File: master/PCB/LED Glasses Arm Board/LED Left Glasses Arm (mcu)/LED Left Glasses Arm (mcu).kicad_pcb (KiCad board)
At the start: 2 copper layers, 131.2 x 17.5 mm, 12 parts, among them J101 Front Connector, J102 SWD, U101 MIC5504-3.3YM5, U102 STM32G071KBU6

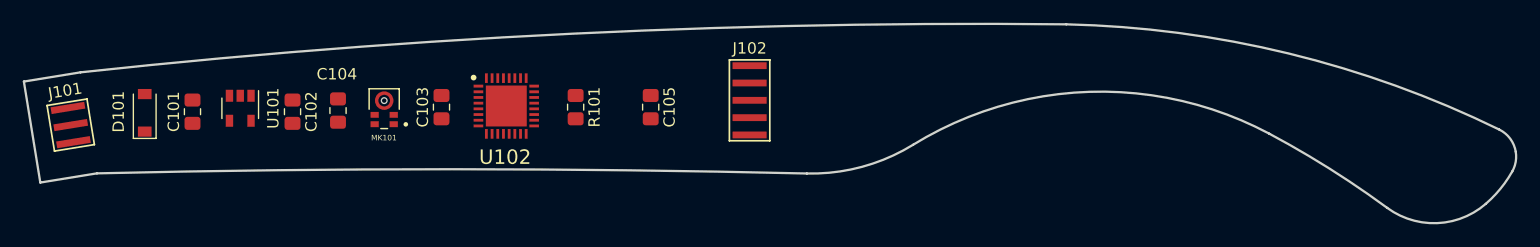
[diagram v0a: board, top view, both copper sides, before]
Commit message: added pushbutton footprint
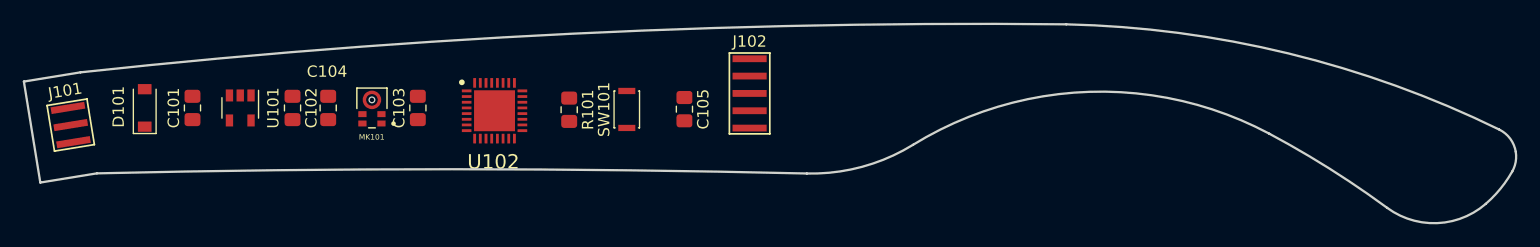
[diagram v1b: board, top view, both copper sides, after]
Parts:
- added SW101: Push Button, Button_Switch_SMD:SW_SPST_CK_KXT3, F.Cu at (133.3, 92.3)
- moved C105 2.97 mm to (138.4, 92.3)
- moved C103 2.08 mm to (114.9, 92.2)
- moved U102 1.12 mm to (121.7, 92.4)
- moved MK101 1.08 mm to (110.9, 92.2)
- moved C104 0.89 mm to (107.0, 92.2)
- moved R101 0.61 mm to (128.2, 92.3)
- moved J102 0.61 mm to (144.1, 89.9)
- moved D101 0.43 mm to (90.9, 92.2)
- moved C101 0.33 mm to (95.1, 92.2)
- moved C102 0.33 mm to (103.9, 92.2)
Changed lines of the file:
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@@
-(kicad_pcb (version 20171130) (host pcbnew "(5.0.0)")
+(kicad_pcb (version 20171130) (host pcbnew "(5.0.1)-3")
   (general
     (thickness 1.6)
@@
     (tracks 0)
     (zones 0)
-    (modules 12)
+    (modules 13)
     (nets 36)
   )
@@
     (add_net "Net-(U102-Pad8)")
   )
+  (module Button_Switch_SMD:SW_SPST_CK_KXT3 (layer F.Cu)
+    (at 133.2992 92.3036 90)
+    (descr https://www.ckswitches.com/media/1465/kxt3.pdf)
+    (tags "Switch SPST KXT3")
+    (attr smd)
+    (fp_text reference SW101 (at 0 -2 90) (layer F.SilkS)
+      (effects (font (size 1 1) (thickness 0.15)))
+    )
+    (fp_text value "Push Button" (at 0 2 90) (layer F.Fab)
+      (effects (font (size 1 1) (thickness 0.15)))
+    )
+    (fp_line (start -1.5 -1) (end 1.5 -1) (layer F.Fab) (width 0.1))
+    (fp_line (start 1.5 -1) (end 1.5 1) (layer F.Fab) (width 0.1))
+    (fp_line (start 1.5 1) (end -1.5 1) (layer F.Fab) (width 0.1))
+    (fp_line (start -1.5 1) (end -1.5 -1) (layer F.Fab) (width 0.1))
+    (fp_line (start 1.5 -0.65) (end 1.75 -0.65) (layer F.Fab) (width 0.1))
+    (fp_line (start 1.75 -0.65) (end 1.75 -0.4) (layer F.Fab) (width 0.1))
+    (fp_line (start 1.75 -0.4) (end 1.5 -0.15) (layer F.Fab) (width 0.1))
+    (fp_line (start 1.5 0.15) (end 1.75 0.4) (layer F.Fab) (width 0.1))
+    (fp_line (start 1.75 0.4) (end 1.75 0.65) (layer F.Fab) (width 0.1))
+    (fp_line (start 1.75 0.65) (end 1.5 0.65) (layer F.Fab) (width 0.1))
+    (fp_line (start -1.5 -0.65) (end -1.75 -0.65) (layer F.Fab) (width 0.1))
+    (fp_line (start -1.75 -0.65) (end -1.75 -0.4) (layer F.Fab) (width 0.1))
+    (fp_line (start -1.75 -0.4) (end -1.5 -0.15) (layer F.Fab) (width 0.1))
+    (fp_line (start -1.5 0.15) (end -1.75 0.4) (layer F.Fab) (width 0.1))
+    (fp_line (start -1.75 0.4) (end -1.75 0.65) (layer F.Fab) (width 0.1))
+    (fp_line (start -1.75 0.65) (end -1.5 0.65) (layer F.Fab) (width 0.1))
+    (fp_text user %R (at 0 0 90) (layer F.Fab)
+      (effects (font (size 0.5 0.5) (thickness 0.075)))
+    )
+    (fp_line (start -1.62 -1.12) (end 1.62 -1.12) (layer F.SilkS) (width 0.12))
+    (fp_line (start 1.62 -1.12) (end 1.62 -1.02) (layer F.SilkS) (width 0.12))
+    (fp_line (start -1.62 -1.12) (end -1.62 -1.02) (layer F.SilkS) (width 0.12))
+    (fp_line (start -1.62 1.12) (end 1.62 1.12) (layer F.SilkS) (width 0.12))
+    (fp_line (start 1.62 1.02) (end 1.62 1.12) (layer F.SilkS) (width 0.12))
+    (fp_line (start -1.62 1.02) (end -1.62 1.12) (layer F.SilkS) (width 0.12))
+    (fp_line (start -2.15 -1.25) (end 2.15 -1.25) (layer F.CrtYd) (width 0.05))
+    (fp_line (start 2.15 -1.25) (end 2.15 1.25) (layer F.CrtYd) (width 0.05))
+    (fp_line (start -2.15 1.25) (end 2.15 1.25) (layer F.CrtYd) (width 0.05))
+    (fp_line (start -2.15 -1.25) (end -2.15 1.25) (layer F.CrtYd) (width 0.05))
+    (pad 1 smd rect (at -1.625 0 90) (size 0.55 1.5) (layers F.Cu F.Paste F.Mask)
+      (net 2 GND))
+    (pad 2 smd rect (at 1.625 0 90) (size 0.55 1.5) (layers F.Cu F.Paste F.Mask)
+      (net 7 /NRST))
+    (model ${KISYS3DMOD}/Button_Switch_SMD.3dshapes/SW_SPST_CK_KXT3.wrl
+      (at (xyz 0 0 0))
+      (scale (xyz 1 1 1))
+      (rotate (xyz 0 0 0))
+    )
+  )
   (module misc-footprints:PinHeader_1x05_P1.00mm_Vertical_SMD_Pin1Left_CUSTOM (layer F.Cu)
-    (at 144.1 90.484)
+    (at 144.1 89.8779)
     (descr "surface-mounted straight pin header, 1x03, 1.00mm pitch, single row, style 1 (pin 1 left)")
     (tags "Surface mounted pin header SMD 1x03 1.00mm single row style1 pin1 left")
@@
   )
   (module misc-footprints:MIC_SPH0641LM4H-1 (layer F.Cu)
-    (at 111.9625 92.236 180)
+    (at 110.8837 92.171199 180)
     (fp_text reference MK101 (at 0.024078 -2.562988 180) (layer F.SilkS)
       (effects (font (size 0.481539 0.481539) (thickness 0.015)))
@@
   )
   (module misc-footprints:QFN50P500X500X60-33N-D (layer F.Cu)
-    (at 122.7 92)
+    (at 121.666 92.4179)
     (descr STM32G071KBU6)
     (tags "Integrated Circuit")
@@
       (effects (font (size 1.27 1.27) (thickness 0.254)))
     )
-    (fp_text user %R (at 0 0) (layer F.Fab)
+    (fp_text user %R (at 0 -0.6016) (layer F.Fab)
       (effects (font (size 1.27 1.27) (thickness 0.254)))
     )
@@
   )
   (module Capacitor_SMD:C_0805_2012Metric_Pad1.15x1.40mm_HandSolder (layer F.Cu)
-    (at 135.4 92.1 270)
+    (at 138.3665 92.2782 270)
     (descr "Capacitor SMD 0805 (2012 Metric), square (rectangular) end terminal, IPC_7351 nominal with elongated pad for handsoldering. (Body size source: https://docs.google.com/spreadsheets/d/1BsfQQcO9C6DZCsRaXUlFlo91Tg2WpOkGARC1WS5S8t0/edit?usp=sharing), generated with kicad-footprint-generator")
     (tags "capacitor handsolder")
@@
   )
   (module Capacitor_SMD:C_0805_2012Metric_Pad1.15x1.40mm_HandSolder (layer F.Cu)
-    (at 107.9 92.4 90)
+    (at 107.0364 92.171199 90)
     (descr "Capacitor SMD 0805 (2012 Metric), square (rectangular) end terminal, IPC_7351 nominal with elongated pad for handsoldering. (Body size source: https://docs.google.com/spreadsheets/d/1BsfQQcO9C6DZCsRaXUlFlo91Tg2WpOkGARC1WS5S8t0/edit?usp=sharing), generated with kicad-footprint-generator")
     (tags "capacitor handsolder")
@@
   )
   (module Capacitor_SMD:C_0805_2012Metric_Pad1.15x1.40mm_HandSolder (layer F.Cu)
-    (at 117 92.1 90)
+    (at 114.9223 92.171199 90)
     (descr "Capacitor SMD 0805 (2012 Metric), square (rectangular) end terminal, IPC_7351 nominal with elongated pad for handsoldering. (Body size source: https://docs.google.com/spreadsheets/d/1BsfQQcO9C6DZCsRaXUlFlo91Tg2WpOkGARC1WS5S8t0/edit?usp=sharing), generated with kicad-footprint-generator")
     (tags "capacitor handsolder")
@@
   )
   (module Capacitor_SMD:C_0805_2012Metric_Pad1.15x1.40mm_HandSolder (layer F.Cu)
-    (at 103.9 92.5 270)
+    (at 103.9 92.171199 270)
     (descr "Capacitor SMD 0805 (2012 Metric), square (rectangular) end terminal, IPC_7351 nominal with elongated pad for handsoldering. (Body size source: https://docs.google.com/spreadsheets/d/1BsfQQcO9C6DZCsRaXUlFlo91Tg2WpOkGARC1WS5S8t0/edit?usp=sharing), generated with kicad-footprint-generator")
     (tags "capacitor handsolder")
@@
   )
   (module Capacitor_SMD:C_0805_2012Metric_Pad1.15x1.40mm_HandSolder (layer F.Cu)
-    (at 95.1 92.5 90)
+    (at 95.1 92.171199 90)
     (descr "Capacitor SMD 0805 (2012 Metric), square (rectangular) end terminal, IPC_7351 nominal with elongated pad for handsoldering. (Body size source: https://docs.google.com/spreadsheets/d/1BsfQQcO9C6DZCsRaXUlFlo91Tg2WpOkGARC1WS5S8t0/edit?usp=sharing), generated with kicad-footprint-generator")
     (tags "capacitor handsolder")
@@
     (fp_line (start 1.85 -0.95) (end 1.85 0.95) (layer F.CrtYd) (width 0.05))
     (fp_line (start 1.85 0.95) (end -1.85 0.95) (layer F.CrtYd) (width 0.05))
-    (fp_text user %R (at 0 0 90) (layer F.Fab)
+    (fp_text user %R (at 0.999999 0 90) (layer F.Fab)
       (effects (font (size 0.5 0.5) (thickness 0.08)))
     )
@@
   )
   (module Diode_SMD:D_SOD-123 (layer F.Cu)
-    (at 90.9 92.6 90)
+    (at 90.9 92.171199 90)
     (descr SOD-123)
     (tags SOD-123)
@@
   )
   (module Package_TO_SOT_SMD:SOT-23-5 (layer F.Cu)
-    (at 99.3 92.2 270)
+    (at 99.3 92.171199 270)
     (descr "5-pin SOT23 package")
     (tags SOT-23-5)
@@
       (effects (font (size 1 1) (thickness 0.15)))
     )
-    (fp_text user %R (at 0 0.2) (layer F.Fab)
+    (fp_text user %R (at -0.73375 0.2) (layer F.Fab)
       (effects (font (size 0.5 0.5) (thickness 0.075)))
     )
@@
   )
   (module Resistor_SMD:R_0805_2012Metric_Pad1.15x1.40mm_HandSolder (layer F.Cu)
-    (at 128.8 92.1 270)
+    (at 128.2319 92.329 270)
     (descr "Resistor SMD 0805 (2012 Metric), square (rectangular) end terminal, IPC_7351 nominal with elongated pad for handsoldering. (Body size source: https://docs.google.com/spreadsheets/d/1BsfQQcO9C6DZCsRaXUlFlo91Tg2WpOkGARC1WS5S8t0/edit?usp=sharing), generated with kicad-footprint-generator")
     (tags "resistor handsolder")
@@
       (effects (font (size 1 1) (thickness 0.15)))
     )
-    (fp_text value "100k, 1/16W" (at 0 1.65 270) (layer F.Fab)
-      (effects (font (size 1 1) (thickness 0.15)))
-    )
+    (fp_text value "100k, 1/16W" (at -0.599999 1.65 270) (layer F.Fab)
+      (effects (font (size 1 1) (thickness 0.15)))
+    )

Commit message: need to reroute but got the basic layout
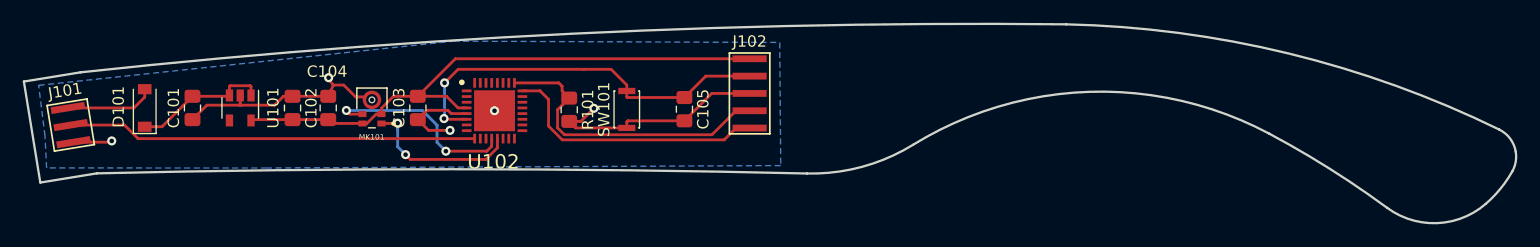
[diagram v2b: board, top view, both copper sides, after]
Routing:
- net +3V3: track 0.00 -> 51.4 mm
- net GND: track 0.00 -> 50.4 mm, vias 0 -> 5
- net /LED_DATA: track 0.00 -> 36.0 mm
- net /NRST: track 0.00 -> 34.9 mm, vias 0 -> 2
- net /SWCLK: track 0.00 -> 26.7 mm
- net /SWDIO: track 0.00 -> 23.6 mm
- net /MIC_CLK: track 0.00 -> 17.5 mm, vias 0 -> 2
- net /MIC_MISO: track 0.00 -> 14.0 mm, vias 0 -> 2
- net Net-(C101-Pad2): track 0.00 -> 12.1 mm
- net Net-(D101-Pad2): track 0.00 -> 7.85 mm
- added copper zone on B.Cu, net GND
